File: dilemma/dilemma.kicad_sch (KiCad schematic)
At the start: 64 parts, among them J1 S3B-PH-SM4-TB(LF)(SN), J2 Serial, J3 BATTERY_CONN_DEANS, J5 S3B-PH-SM4-TB(LF)(SN), J7 trackball, SW1 SW_Push, SW10 SW_Push, SW11 SW_Push, SW12 SW_Push, SW13 SW_Push, SW14 SW_Push, SW15 SW_Push, SW16 SW_Push, SW17 SW_Push, SW2 SW_Push, SW26 SW_SPST, SW3 SW_Push, SW37 SW_SPST, SW4 SW_Push, SW5 SW_Push, SW6 SW_Push, SW7 SW_Push, SW8 SW_Push, SW9 SW_Push, U2 eliteC

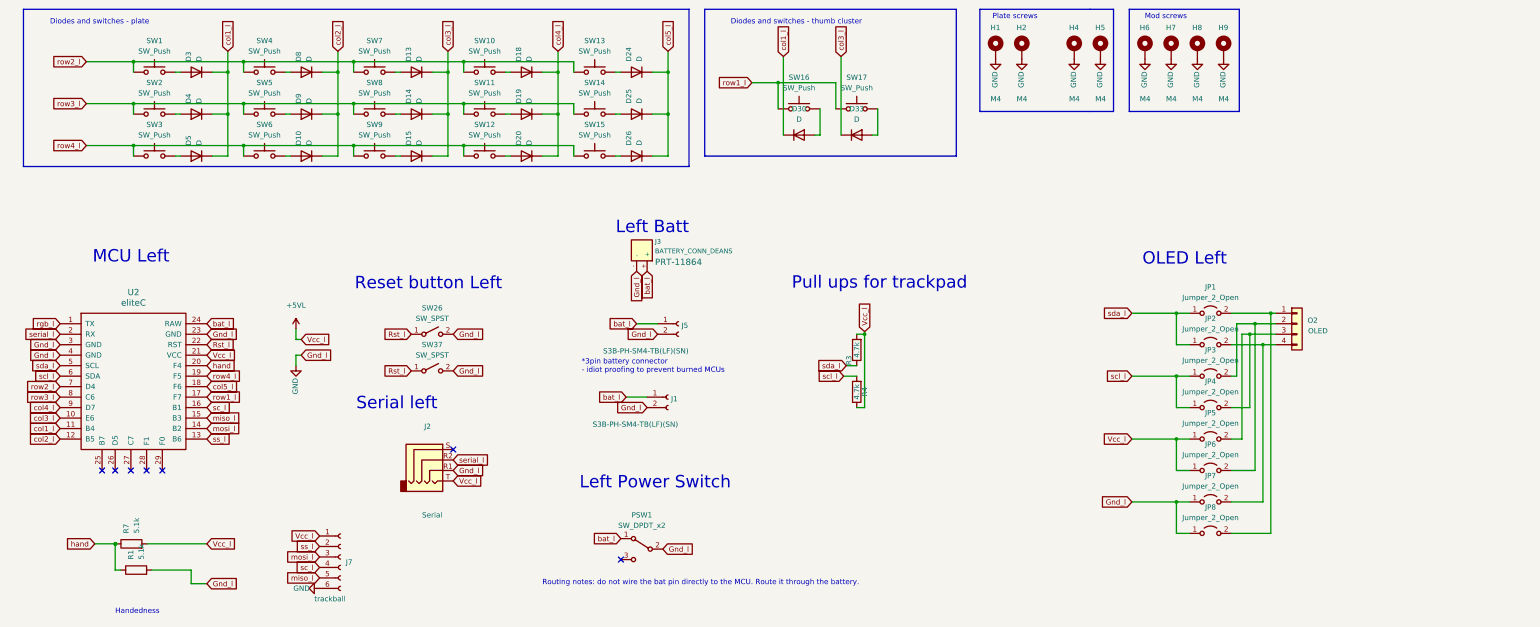
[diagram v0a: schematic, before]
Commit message: add serial jumper
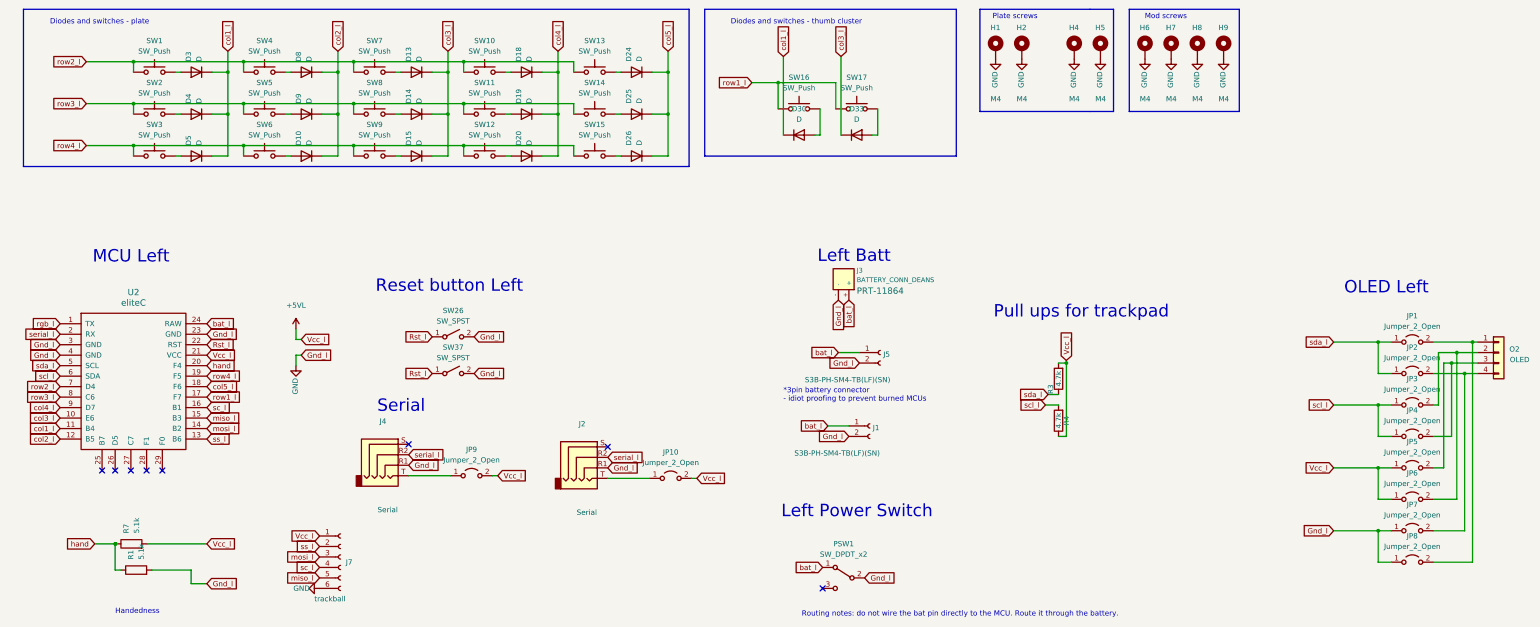
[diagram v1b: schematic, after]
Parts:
- added J4: Serial, local-libraries:Jack_3.5mm_PJ320E_Horizontal_custom, symbol Connector:AudioJack4
- added JP10, JP9: Jumper_2_Open, local-libraries:SolderJumper-2_P1.3mm_Open_RoundedPad1.0x1.5mm, symbol Jumper:Jumper_2_Open
- J2: footprint local-libraries:Jack_3.5mm_PJ320E_Horizontal_reversible -> local-libraries:Jack_3.5mm_PJ320E_Horizontal_custom
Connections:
- net +5VL: now also JP10.2 (B), JP9.2 (B); no longer J2.T
- net GND: now also J4.R1
- net serial_l: now also J4.R2
- new net: J2.T, JP10.1 (A)
- new net: J4.T, JP9.1 (A)
- no-connect marks 7 -> 8
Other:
- note added: "Serial"
- note removed: "Serial left"
- moved on the sheet: J1, J2, J3, J5, JP1, JP2, JP3, JP4, JP5, JP6, JP7, JP8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
